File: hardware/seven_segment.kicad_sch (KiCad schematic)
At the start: 36 parts, among them J1 Conn_01x16, J2 PJ-102AH, J3 Conn_01x04, J5 Conn_01x06, SW2 SW_Push, U1 ESP32-WROOM-32E, U2 ULN2003A, U3 ULN2003A, U4 TPS562200, U5 74HC595, U6 74HC595, U7 ULN2003A

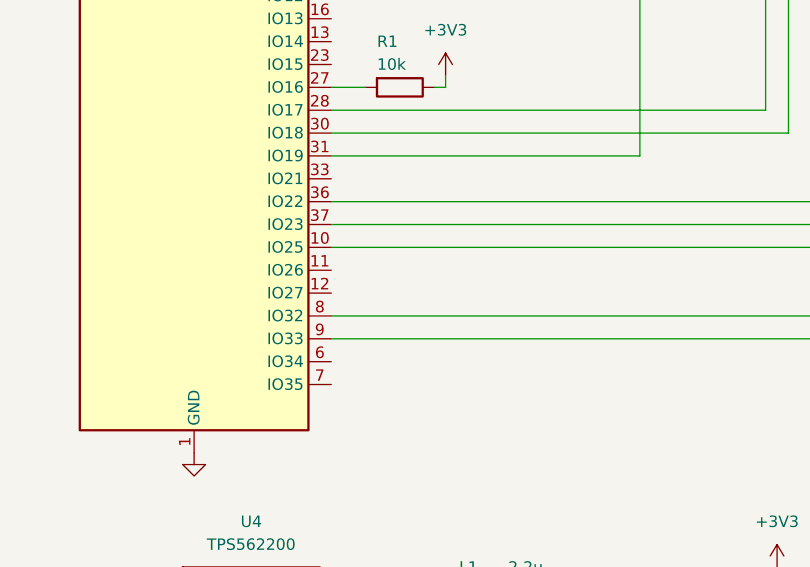
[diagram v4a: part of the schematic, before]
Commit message: hardware: Add net labels to SPI channel
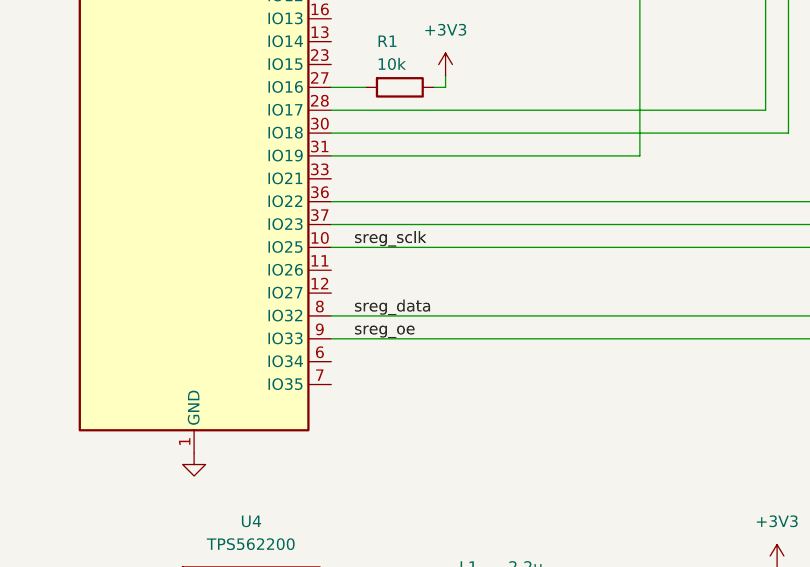
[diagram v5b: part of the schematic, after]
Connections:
- net sreg_sclk: now reaches U1.10 (IO25), U5.11 (SRCLK), U5.12 (RCLK), U6.11 (SRCLK), U6.12 (RCLK)
- net sreg_oe: now reaches U1.9 (IO33), U5.13 (~{OE}), U6.13 (~{OE})
- net sreg_data: now reaches U1.8 (IO32), U5.14 (SER)
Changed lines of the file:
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@@
+		)
+	)
+	(label "sreg_oe"
+		(at 106.68 138.43 0)
+		(effects
+			(font
+				(size 1.27 1.27)
+			)
+			(justify left bottom)
+		)
+	)
+	(label "sreg_sclk"
+		(at 106.68 128.27 0)
+		(effects
+			(font
+				(size 1.27 1.27)
+			)
+			(justify left bottom)
 		)
 	)
@@
 		(effects
 			(font
+				(size 1.27 1.27)
+			)
+			(justify left bottom)
+		)
+	)
+	(label "sreg_data"
+		(at 106.68 135.89 0)
+		(effects
+			(font

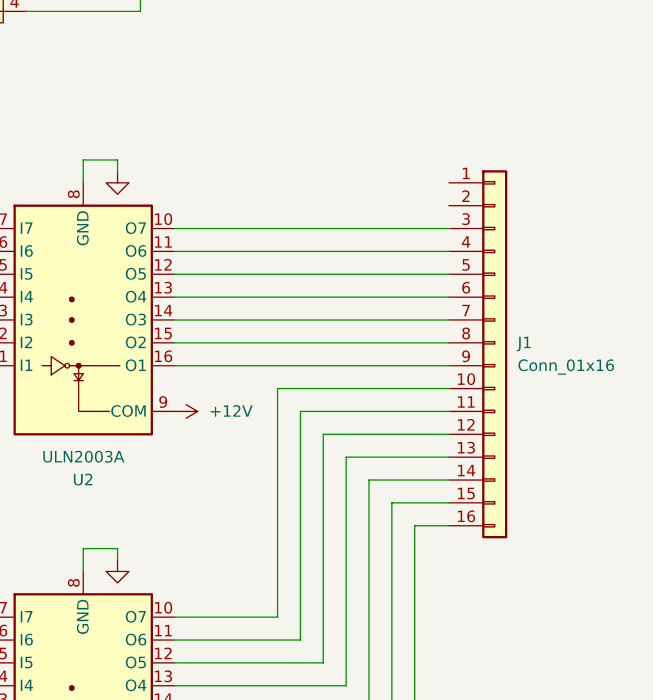
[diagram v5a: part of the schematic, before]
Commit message: hardware: Add net labels to segment control pins
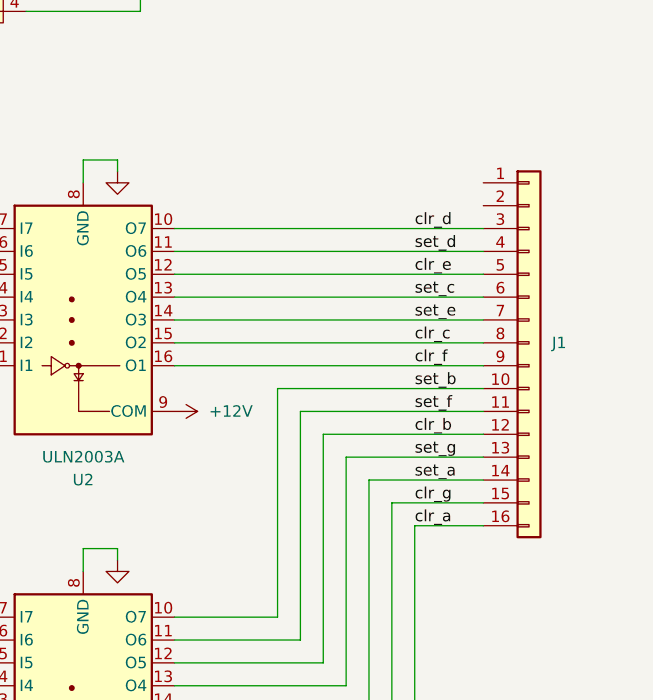
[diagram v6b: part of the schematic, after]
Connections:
- net set_b: now reaches J1.10 (Pin_10), U3.10 (O7)
- net set_f: now reaches J1.11 (Pin_11), U3.11 (O6)
- net clr_b: now reaches J1.12 (Pin_12), U3.12 (O5)
- net set_g: now reaches J1.13 (Pin_13), U3.13 (O4)
- net set_a: now reaches J1.14 (Pin_14), U3.14 (O3)
- net clr_g: now reaches J1.15 (Pin_15), U3.15 (O2)
- net clr_a: now reaches J1.16 (Pin_16), U3.16 (O1)
- net clr_d: now reaches J1.3 (Pin_3), U2.10 (O7)
- net set_d: now reaches J1.4 (Pin_4), U2.11 (O6)
- net clr_e: now reaches J1.5 (Pin_5), U2.12 (O5)
- net set_c: now reaches J1.6 (Pin_6), U2.13 (O4)
- net set_e: now reaches J1.7 (Pin_7), U2.14 (O3)
- net clr_c: now reaches J1.8 (Pin_8), U2.15 (O2)
- net clr_f: now reaches J1.9 (Pin_9), U2.16 (O1)
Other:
- moved on the sheet: J1
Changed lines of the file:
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@@
 	(wire
 		(pts
-			(xy 261.62 97.79) (xy 231.14 97.79)
+			(xy 265.43 97.79) (xy 231.14 97.79)
 		)
 		(stroke
@@
 	(wire
 		(pts
-			(xy 247.65 115.57) (xy 261.62 115.57)
+			(xy 247.65 115.57) (xy 265.43 115.57)
 		)
 		(stroke
@@
 	(wire
 		(pts
+			(xy 231.14 95.25) (xy 265.43 95.25)
+		)
+		(stroke
+			(width 0)
+			(type default)
+		)
+	)
+	(wire
+		(pts
 			(xy 205.74 107.95) (xy 210.82 107.95)
 		)
@@
 	(wire
 		(pts
-			(xy 261.62 102.87) (xy 231.14 102.87)
+			(xy 250.19 143.51) (xy 250.19 118.11)
 		)
 		(stroke
@@
 	(wire
 		(pts
-			(xy 250.19 143.51) (xy 250.19 118.11)
+			(xy 252.73 120.65) (xy 265.43 120.65)
 		)
 		(stroke
@@
 	(wire
 		(pts
-			(xy 252.73 120.65) (xy 261.62 120.65)
+			(xy 205.74 151.13) (xy 210.82 151.13)
 		)
 		(stroke
@@
 	(wire
 		(pts
-			(xy 205.74 151.13) (xy 210.82 151.13)
+			(xy 193.04 39.37) (xy 193.04 53.34)
 		)
 		(stroke
@@
 	(wire
 		(pts
-			(xy 193.04 39.37) (xy 193.04 53.34)
+			(xy 231.14 102.87) (xy 265.43 102.87)
 		)
 		(stroke
@@
 	(wire
 		(pts
-			(xy 242.57 110.49) (xy 261.62 110.49)
+			(xy 242.57 110.49) (xy 265.43 110.49)
 		)
 		(stroke
@@
 	(wire
 		(pts
-			(xy 245.11 113.03) (xy 261.62 113.03)
+			(xy 245.11 113.03) (xy 265.43 113.03)
 		)
 		(stroke
@@
 	(wire
 		(pts
-			(xy 261.62 95.25) (xy 231.14 95.25)
-		)
-		(stroke
-			(width 0)
-			(type default)
-		)
-	)
-	(wire
-		(pts
 			(xy 220.98 128.27) (xy 220.98 130.81)
 		)
@@
 	(wire
 		(pts
-			(xy 250.19 118.11) (xy 261.62 118.11)
+			(xy 250.19 118.11) (xy 265.43 118.11)
 		)
 		(stroke
@@
 	(wire
 		(pts
-			(xy 261.62 105.41) (xy 231.14 105.41)
+			(xy 265.43 105.41) (xy 231.14 105.41)
 		)
 		(stroke
@@
 	(wire
 		(pts
-			(xy 261.62 92.71) (xy 231.14 92.71)
+			(xy 265.43 92.71) (xy 231.14 92.71)
 		)
 		(stroke
@@
 	(wire
 		(pts
-			(xy 257.81 125.73) (xy 261.62 125.73)
+			(xy 257.81 125.73) (xy 265.43 125.73)
 		)
 		(stroke
@@
 	(wire
 		(pts
-			(xy 255.27 123.19) (xy 261.62 123.19)
+			(xy 255.27 123.19) (xy 265.43 123.19)
 		)
 		(stroke
@@
 	(wire
 		(pts
-			(xy 261.62 107.95) (xy 231.14 107.95)
+			(xy 265.43 107.95) (xy 231.14 107.95)
 		)
 		(stroke
@@
 	(wire
 		(pts
-			(xy 261.62 100.33) (xy 231.14 100.33)
+			(xy 175.26 105.41) (xy 185.42 105.41)
 		)
 		(stroke
@@
 	(wire
 		(pts
-			(xy 175.26 105.41) (xy 185.42 105.41)
+			(xy 231.14 100.33) (xy 265.43 100.33)
 		)
 		(stroke
@@
 		)
 	)
+	(label "clr_d"
+		(at 257.81 92.71 0)
+		(effects
+			(font
+				(size 1.27 1.27)
+			)
+			(justify left bottom)
+		)
+	)
+	(label "set_d"
+		(at 257.81 95.25 0)
+		(effects
+			(font
+				(size 1.27 1.27)
+			)
+			(justify left bottom)
+		)
+	)
+	(label "set_b"
+		(at 257.81 110.49 0)
+		(effects
+			(font
+				(size 1.27 1.27)
+			)
+			(justify left bottom)
+		)
+	)
+	(label "clr_e"
+		(at 257.81 97.79 0)
+		(effects
+			(font
+				(size 1.27 1.27)
+			)
+			(justify left bottom)
+		)
+	)
+	(label "clr_c"
+		(at 257.81 105.41 0)
+		(effects
+			(font
+				(size 1.27 1.27)
+			)
+			(justify left bottom)
+		)
+	)
 	(label "TXD0"
 		(at 106.68 87.63 0)
@@
 		)
 	)
+	(label "clr_a"
+		(at 257.81 125.73 0)
+		(effects
+			(font
+				(size 1.27 1.27)
+			)
+			(justify left bottom)
+		)
+	)
+	(label "clr_f"
+		(at 257.81 107.95 0)
+		(effects
+			(font
+				(size 1.27 1.27)
+			)
+			(justify left bottom)
+		)
+	)
 	(label "sreg_sclk"
 		(at 106.68 128.27 0)
@@
 		)
 	)
+	(label "set_a"
+		(at 257.81 120.65 0)
+		(effects
+			(font
+				(size 1.27 1.27)
+			)
+			(justify left bottom)
+		)
+	)
+	(label "clr_g"
+		(at 257.81 123.19 0)
+		(effects
+			(font
+				(size 1.27 1.27)
+			)
+			(justify left bottom)
+		)
+	)
+	(label "set_c"
+		(at 257.81 100.33 0)
+		(effects
+			(font
+				(size 1.27 1.27)
+			)
+			(justify left bottom)
+		)
+	)
+	(label "clr_b"
+		(at 257.81 115.57 0)
+		(effects
+			(font
+				(size 1.27 1.27)
+			)
+			(justify left bottom)
+		)
+	)
 	(label "sreg_data"
 		(at 106.68 135.89 0)
@@
 		)
 	)
+	(label "set_g"
+		(at 257.81 118.11 0)
+		(effects
+			(font
+				(size 1.27 1.27)
+			)
+			(justify left bottom)
+		)
+	)
+	(label "set_e"
+		(at 257.81 102.87 0)
+		(effects
+			(font
+				(size 1.27 1.27)
+			)
+			(justify left bottom)
+		)
+	)
+	(label "set_f"
+		(at 257.81 113.03 0)
+		(effects
+			(font
+				(size 1.27 1.27)
+			)
+			(justify left bottom)
+		)
+	)
 	(symbol
 		(lib_id "00_customsymbols:Relay")
@@
 	(symbol
 		(lib_id "Connector_Generic:Conn_01x16")
-		(at 266.7 105.41 0)
+		(at 270.51 105.41 0)
 		(unit 1)
 		(exclude_from_sim no)
@@
 		(fields_autoplaced yes)
 		(property "Reference" "J1"
-			(at 269.24 105.4099 0)
+			(at 273.05 105.4099 0)
 			(effects
 				(font
@@
 		)
 		(property "Value" "Conn_01x16"
-			(at 269.24 107.9499 0)
+			(at 273.05 107.9499 0)
 			(effects
 				(font
@@
 				)
 				(justify left)
+				(hide yes)
 			)
 		)
 		(property "Footprint" "Connector_PinHeader_2.54mm:PinHeader_2x08_P2.54mm_Vertical"
-			(at 266.7 105.41 0)
+			(at 270.51 105.41 0)
 			(effects
 				(font
@@
 		)
 		(property "Datasheet" "~"
-			(at 266.7 105.41 0)
+			(at 270.51 105.41 0)
 			(effects
 				(font
@@
 		)
 		(property "Description" ""
-			(at 266.7 105.41 0)
+			(at 270.51 105.41 0)
 			(effects
 				(font
